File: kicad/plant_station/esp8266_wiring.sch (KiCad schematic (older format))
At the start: 17 parts, among them J6 Conn_01x03_POWER_JUMPER, P1 USB_C_Plug_USB2.0, SW1 SW_RESET, SW2 SW_FLASH, U3 CP2102N-A01-GQFN28, U4 ESP-WROOM-02

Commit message: Started working on v3 - added ADC081 driver and removed CAP and IQS chips
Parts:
- Cdec6, Cdec7: footprint Capacitor_SMD:C_1206_3216Metric -> (none)
- R17: value 10K -> 4K7
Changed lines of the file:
@@
 P 7800 1450
 F 0 "R17" H 7870 1496 50  0000 L CNN
-F 1 "10K" H 7870 1405 50  0000 L CNN
+F 1 "4K7" H 7870 1405 50  0000 L CNN
 F 2 "Resistor_SMD:R_1206_3216Metric" V 7730 1450 50  0001 C CNN
 F 3 "~" H 7800 1450 50  0001 C CNN
@@
 F 0 "Cdec7" H 6300 1600 50  0000 L CNN
 F 1 "4.7μF" H 6300 1400 50  0000 L CNN
-F 2 "Capacitor_SMD:C_1206_3216Metric" H 6588 1350 50  0001 C CNN
+F 2 "" H 6588 1350 50  0001 C CNN
 F 3 "~" H 6550 1500 50  0001 C CNN
 	1    6550 1500
@@
 P 5850 1050
 F 0 "J6" V 5814 862 50  0000 R CNN
-F 1 "Conn_01x03_POWER_JUMPER" V 5723 862 50  0000 R CNN
+F 1 "Conn_01x03_POWER_JUMPER" V 6000 1600 50  0000 R CNN
 F 2 "Connector_PinHeader_2.54mm:PinHeader_1x03_P2.54mm_Vertical" H 5850 1050 50  0001 C CNN
 F 3 "~" H 5850 1050 50  0001 C CNN
@@
 F 0 "Cdec6" H 4600 1350 50  0000 L CNN
 F 1 "4.7μF" H 4600 1150 50  0000 L CNN
-F 2 "Capacitor_SMD:C_1206_3216Metric" H 4888 1100 50  0001 C CNN
+F 2 "" H 4888 1100 50  0001 C CNN
 F 3 "~" H 4850 1250 50  0001 C CNN
 	1    4850 1250

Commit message: v3 schematics complete, USB breakout PCB designed
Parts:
- removed Cdec5, Cdec8: 0.1μF, Capacitor_SMD:C_1206_3216Metric, symbol Device:C
- removed Cdec6, Cdec7: 4.7μF, symbol Device:C
- removed D2: SP0503BAHT, Package_TO_SOT_SMD:SOT-143, symbol Power_Protection:SP0503BAHT
- removed J6: Conn_01x03_POWER_JUMPER, Connector_PinHeader_2.54mm:PinHeader_1x03_P2.54mm_Vertical, symbol Connector_Generic:Conn_01x03
- removed P1: USB_C_Plug_USB2.0, Connector_USB:USB_C_Receptacle_Amphenol_12401610E4-2A, symbol Connector:USB_C_Plug_USB2.0
- removed R14: 22K1, Resistor_SMD:R_0805_2012Metric, symbol Device:R
- removed R15: 47K5, Resistor_SMD:R_0805_2012Metric, symbol Device:R
- removed R16: 4K7, Resistor_SMD:R_0805_2012Metric, symbol Device:R
- removed R18: 10K, Resistor_SMD:R_1206_3216Metric, symbol Device:R
- removed SW1: SW_RESET, Button_Switch_SMD:SW_SPST_PTS810, symbol Switch:SW_Push
- removed SW2: SW_FLASH, Button_Switch_SMD:SW_SPST_PTS810, symbol Switch:SW_Push
- removed U3: CP2102N-A01-GQFN28, Package_DFN_QFN:QFN-28-1EP_5x5mm_P0.5mm_EP3.35x3.35mm, symbol Interface_USB:CP2102N-A01-GQFN28
- added C10: 220uF, Capacitor_Tantalum_SMD:CP_EIA-3216-18_Kemet-A, symbol Device:CP
- added C6: 0.1μF, Capacitor_SMD:C_1206_3216Metric, symbol Device:C
- added C8: 0.1uF, Capacitor_SMD:C_1206_3216Metric, symbol Device:C
- added D2: LS4148, Parts:MELF_SOD_80_3_BZT55B13GS08, symbol Device:D
- added J1: Conn_02x08_Odd_Even, Connector_PinHeader_2.54mm:PinHeader_2x08_P2.54mm_Vertical, symbol Connector_Generic:Conn_02x08_Odd_Even
- added J17, J18: Conn_01x08, Connector_PinHeader_2.54mm:PinHeader_1x08_P2.54mm_Vertical, symbol Connector_Generic:Conn_01x08
- added J8: Conn_01x06, Connector_PinHeader_2.54mm:PinHeader_1x06_P2.54mm_Vertical, symbol Connector_Generic:Conn_01x06
- added Q4: DMG2301L, Package_TO_SOT_SMD:SOT-23, symbol Transistor_FET:DMG2301L
- added R10, R12, R13, R7: 10K, Resistor_SMD:R_0805_2012Metric, symbol Device:R
- added R2: 16.9K, Resistor_SMD:R_0805_2012Metric, symbol Device:R
- added R3, R9: 4K7, Resistor_SMD:R_0805_2012Metric, symbol Device:R
- added R6: 97.6K, Resistor_SMD:R_0805_2012Metric, symbol Device:R
- added U5: TPL5110, Package_TO_SOT_SMD:SOT-23-6, symbol Timer:TPL5110
- R17: value 4K7 -> 10K; footprint Resistor_SMD:R_1206_3216Metric -> Resistor_SMD:R_0805_2012Metric
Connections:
- net labels added: ALL_EN, ESP_EN, ESP_RST, HOST_WAKE_UP, USB_RXD, USB_TXD, VDD, WAKE_UP
- wire segments 69 -> 37
- no-connect marks 22 -> 4
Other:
- note added: "Config and pull"
- note added: "External USB-UART"
- note added: "GPIO"
- note added: "GPIO16 is connected to WAKE_UP line.\nIf uC wants to stay awake - it pulls it down \nso the TPL timer keeps driving power.\nUseful for e.g. setting up or OTA."
- note added: "Host Wake Up (active high)"
- note added: "I2C Pull Up"
- note added: "Logic IO"
- note added: "Tip=20s, Rext=14.41K (16.9 / 97.6)\nTip=20m, Rext=77.57K (140.0 / 174.0)"
- moved on the sheet: C9, R17, U4

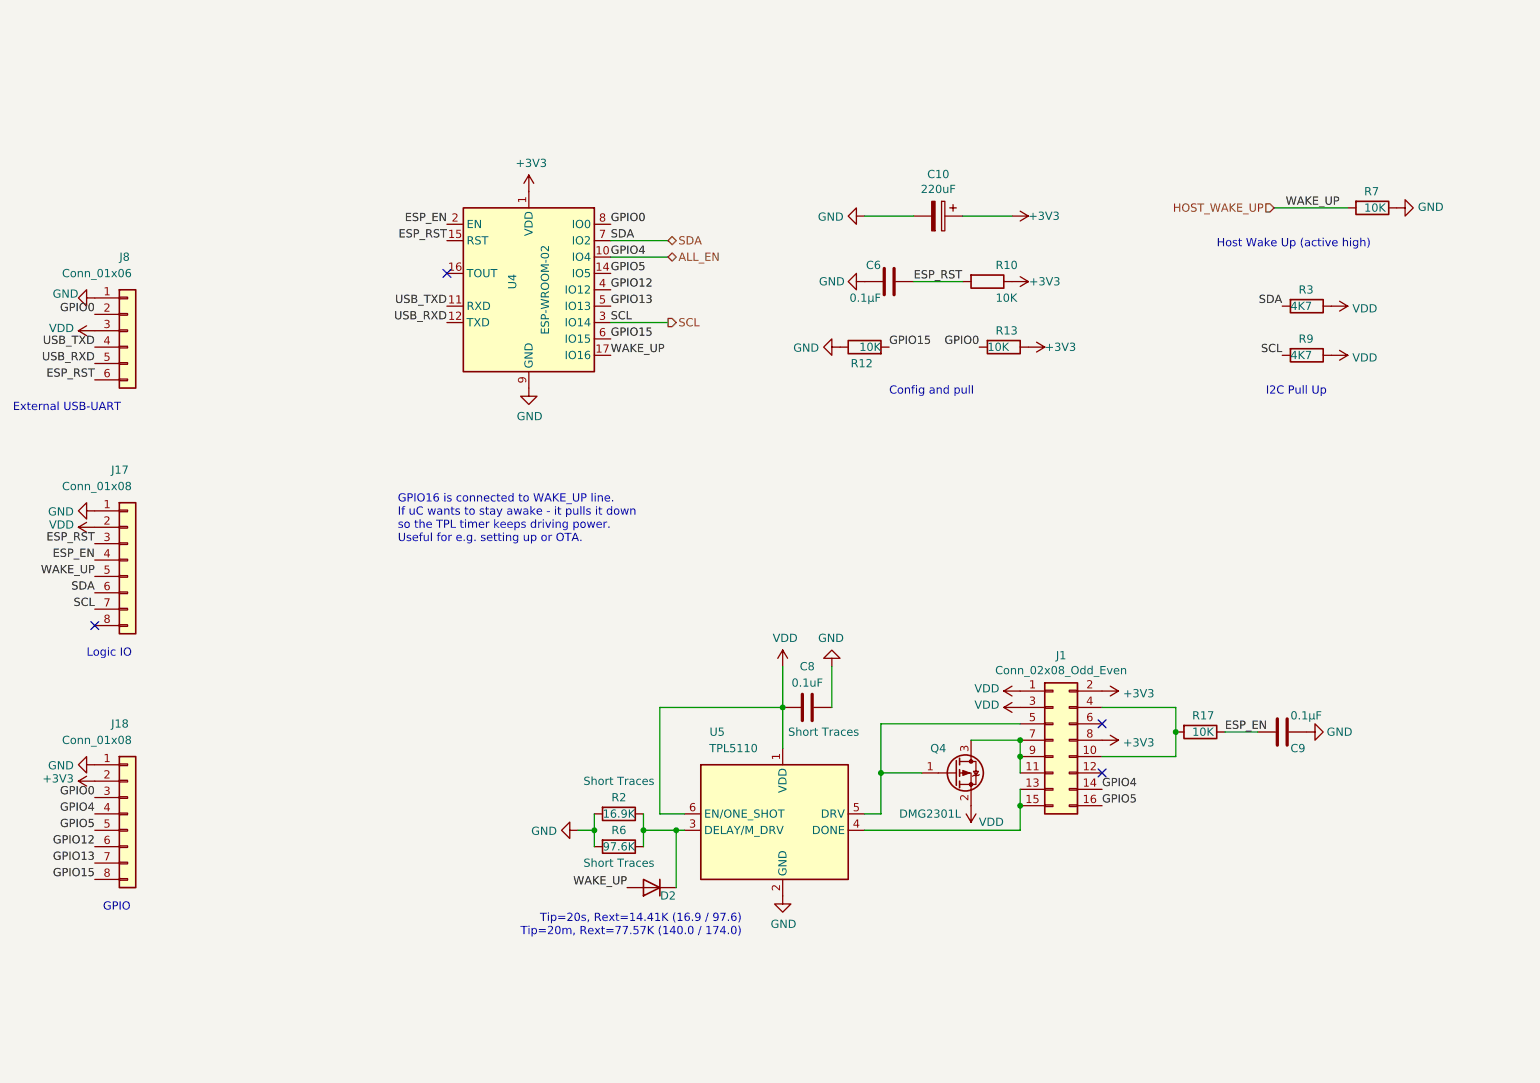
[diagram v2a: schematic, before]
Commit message: Moved the LED driver to LEDs board, refactored connectors. Hopefuly PCBNEW could update it all in place
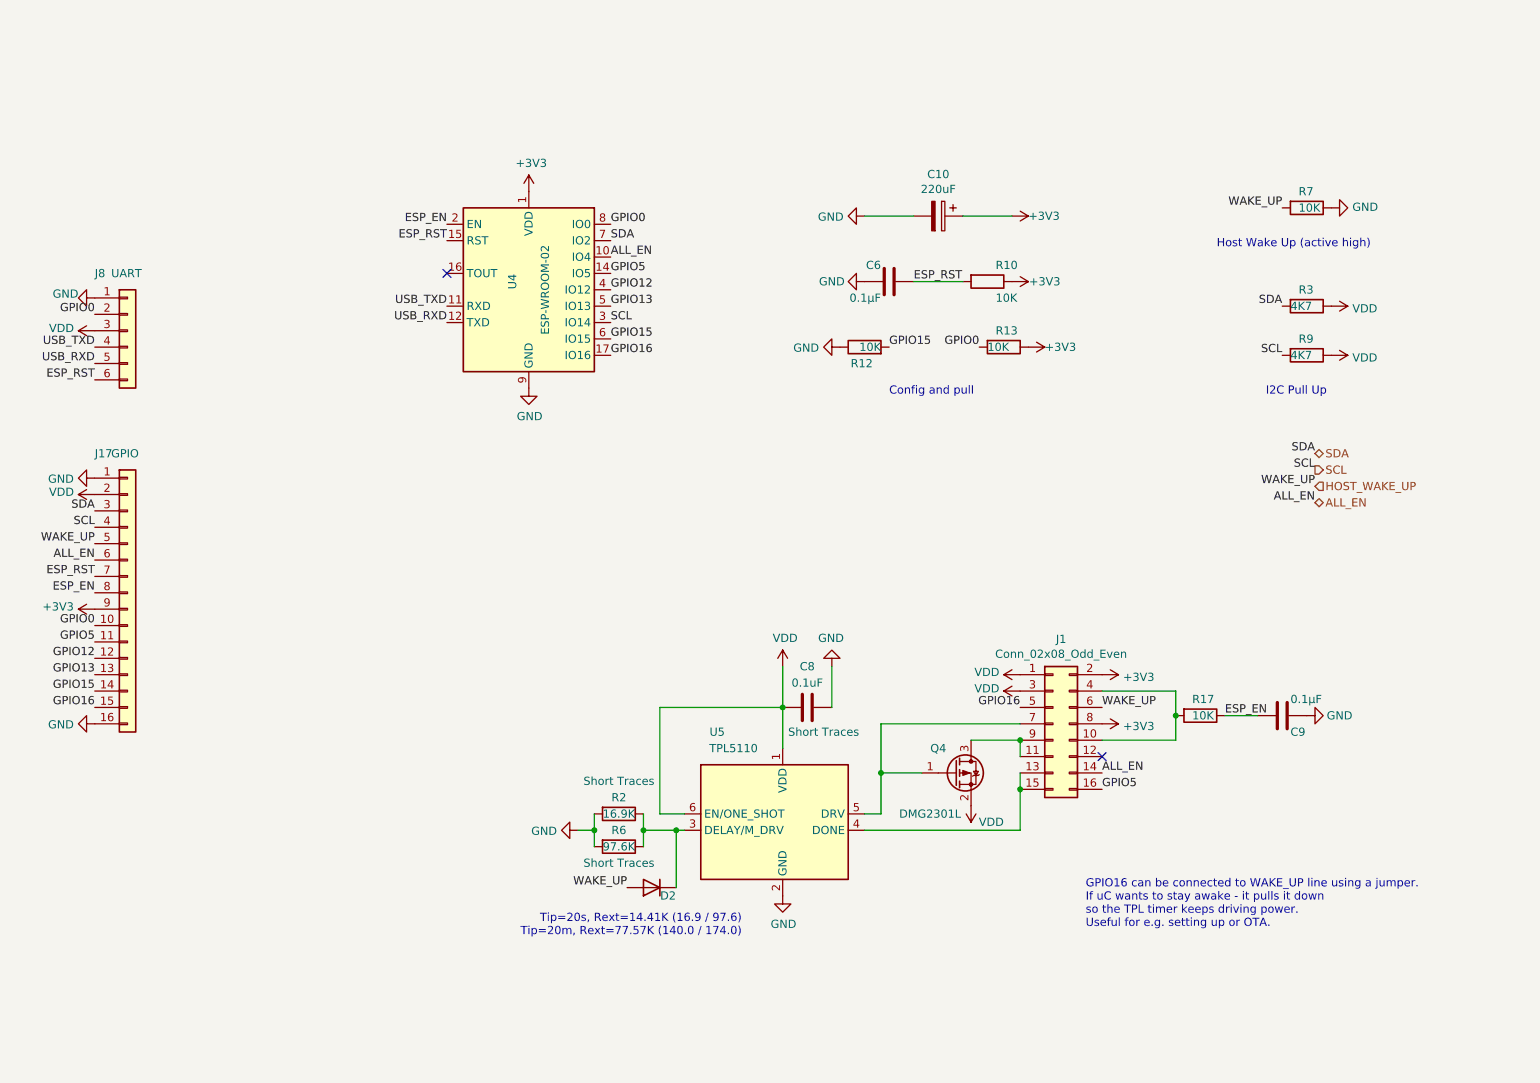
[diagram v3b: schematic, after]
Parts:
- removed J17, J18: Conn_01x08, Connector_PinHeader_2.54mm:PinHeader_1x08_P2.54mm_Vertical, symbol Connector_Generic:Conn_01x08
- added J17: GPIO, Connector_PinHeader_2.54mm:PinHeader_1x16_P2.54mm_Vertical, symbol Connector_Generic:Conn_01x16
- J8: value Conn_01x06 -> UART
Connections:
- net +3V3: now also J17.9 (Pin_9)
- net ALL_EN: now also J17.6 (Pin_6)
- net ESP_EN: now also J17.8 (Pin_8)
- net ESP_RST: now also J17.7 (Pin_7)
- net GND: now also J17.1 (Pin_1), J17.16 (Pin_16)
- net GPIO0: now also J17.10 (Pin_10)
- net GPIO12: now also J17.12 (Pin_12)
- net GPIO13: now also J17.13 (Pin_13)
- net GPIO15: now also J17.14 (Pin_14)
- net GPIO5: now also J17.11 (Pin_11)
- net HOST_WAKE_UP: now also J1.6 (Pin_6), J17.5 (Pin_5); no longer U4.17 (IO16)
- net SCL: now also J17.4 (Pin_4)
- net SDA: now also J17.3 (Pin_3)
- net VDD: now also J17.2 (Pin_2)
- net at Q4.1 (G), U5.5 (DRV): now also J1.7 (Pin_7); no longer J1.5 (Pin_5)
- net at J1.11 (Pin_11), J1.9 (Pin_9), Q4.3 (D): no longer J1.7 (Pin_7)
- new net GPIO16: J1.5 (Pin_5), J17.15 (Pin_15), U4.17 (IO16)
- no-connect marks 4 -> 2
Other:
- note added: "GPIO16 can be connected to WAKE_UP line using a jumper.\nIf uC wants to stay awake - it pulls it down \nso the TPL timer keeps driving power.\nUseful for e.g. setting up or OTA."
- note removed: "External USB-UART"
- note removed: "GPIO"
- note removed: "GPIO16 is connected to WAKE_UP line.\nIf uC wants to stay awake - it pulls it down \nso the TPL timer keeps driving power.\nUseful for e.g. setting up or OTA."
- note removed: "Logic IO"
- moved on the sheet: C9, J1, R17, R7
